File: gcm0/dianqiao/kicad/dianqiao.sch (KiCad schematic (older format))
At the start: 84 parts, among them J1 Conn_Coaxial, J2 Conn_Coaxial, J3 Conn_Coaxial, J4 Conn_Coaxial, SW1 2, SW2 0, SW3 1, U1 NE5532, U10 TL084, U11 NE5532, U12 NE5532, U2 LM2596T-ADJ, U3 LM1117-3.3, U4 LM7805_TO220, U5 STM32F030F4P6, U6 CD4052B, U7 NE5532, U8 CD4053B, U9 74HC595, Y1 8M

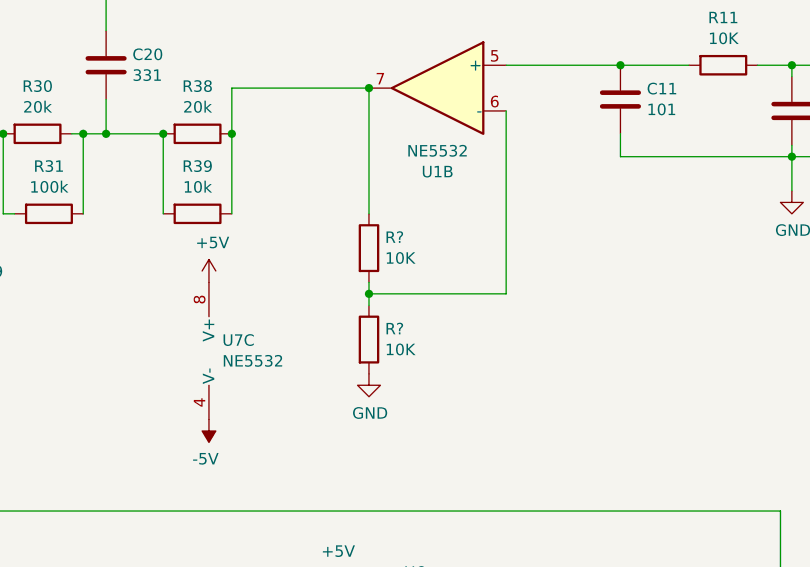
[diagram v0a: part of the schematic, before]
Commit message: 电感显示
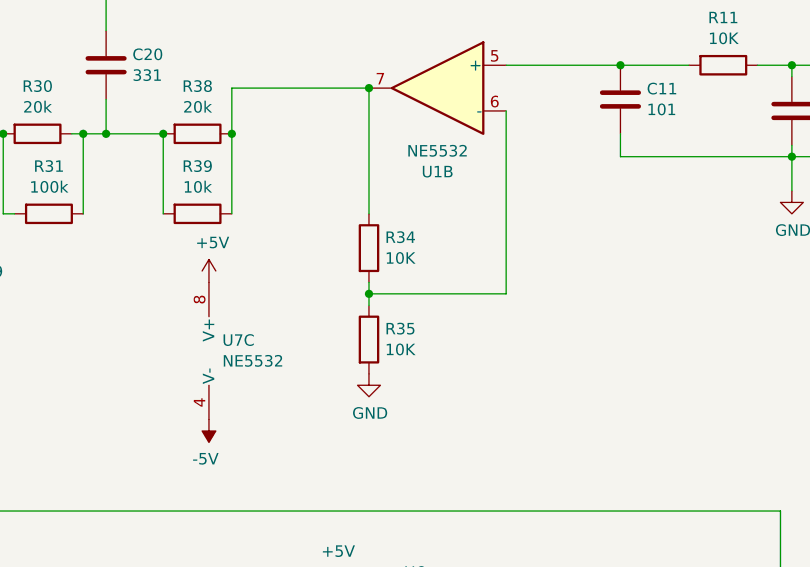
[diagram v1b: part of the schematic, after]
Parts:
- C1: footprint (none) -> Capacitor_THT:CP_Radial_D10.0mm_P7.50mm
- C10, C11, C12, C13, C14, C16, C17, C18, C19, C20, C21, C6, C7, C9: footprint (none) -> Capacitor_THT:C_Axial_L12.0mm_D6.5mm_P15.00mm_Horizontal
- C15, C5, C8: footprint (none) -> Capacitor_THT:CP_Axial_L20.0mm_D10.0mm_P26.00mm_Horizontal
- C2: footprint (none) -> Capacitor_THT:C_Rect_L7.0mm_W4.5mm_P5.00mm
- C3: footprint (none) -> Capacitor_THT:CP_Radial_D13.0mm_P2.50mm
- C4: footprint (none) -> Capacitor_THT:C_Disc_D6.0mm_W4.4mm_P5.00mm
- D1: footprint Diode_THT:D_DO-201AD_P15.24mm_Horizontal -> Diode_THT:D_DO-201AD_P5.08mm_Vertical_AnodeUp
- J1, J2, J3, J4: footprint (none) -> Connector_Coaxial:SMA_Amphenol_901-144_Vertical
- L1: footprint (none) -> Inductor_SMD:L_7.3x7.3_H3.5
- R1, R10, R11, R12, R13, R14, R15, R16, R17, R18, R19, R2, R20, R21, R22, R23, R24, R25, R26, R27, R28, R29, R3, R30, R31, R32, R33, R36, R37, R38, R39, R4, R5, R6, R7, R8, R9: footprint (none) -> Resistor_THT:R_Axial_DIN0207_L6.3mm_D2.5mm_P10.16mm_Horizontal
- R34, R35: renamed from R?; footprint (none) -> Resistor_THT:R_Axial_DIN0207_L6.3mm_D2.5mm_P10.16mm_Horizontal
- R40: footprint (none) -> Resistor_THT:R_Axial_DIN0207_L6.3mm_D2.5mm_P7.62mm_Horizontal
- SW1, SW2, SW3: footprint (none) -> Battery:BatteryHolder_Keystone_107_1x23mm
- U1, U11, U12, U7: footprint (none) -> Package_DIP:DIP-8_W7.62mm
- U10: footprint (none) -> Package_DIP:DIP-14_W7.62mm
- U3: footprint (none) -> Package_TO_SOT_SMD:SOT-223-3_TabPin2
- U6, U8, U9: footprint (none) -> Package_DIP:DIP-16_W7.62mm
- Y1: footprint (none) -> Crystal:Crystal_HC49-U_Vertical
